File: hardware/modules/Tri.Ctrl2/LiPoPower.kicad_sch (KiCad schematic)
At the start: 26 parts, among them SW901 Power Switch, U901 INA226, U902 TPS63070RNMR, U903 INA226

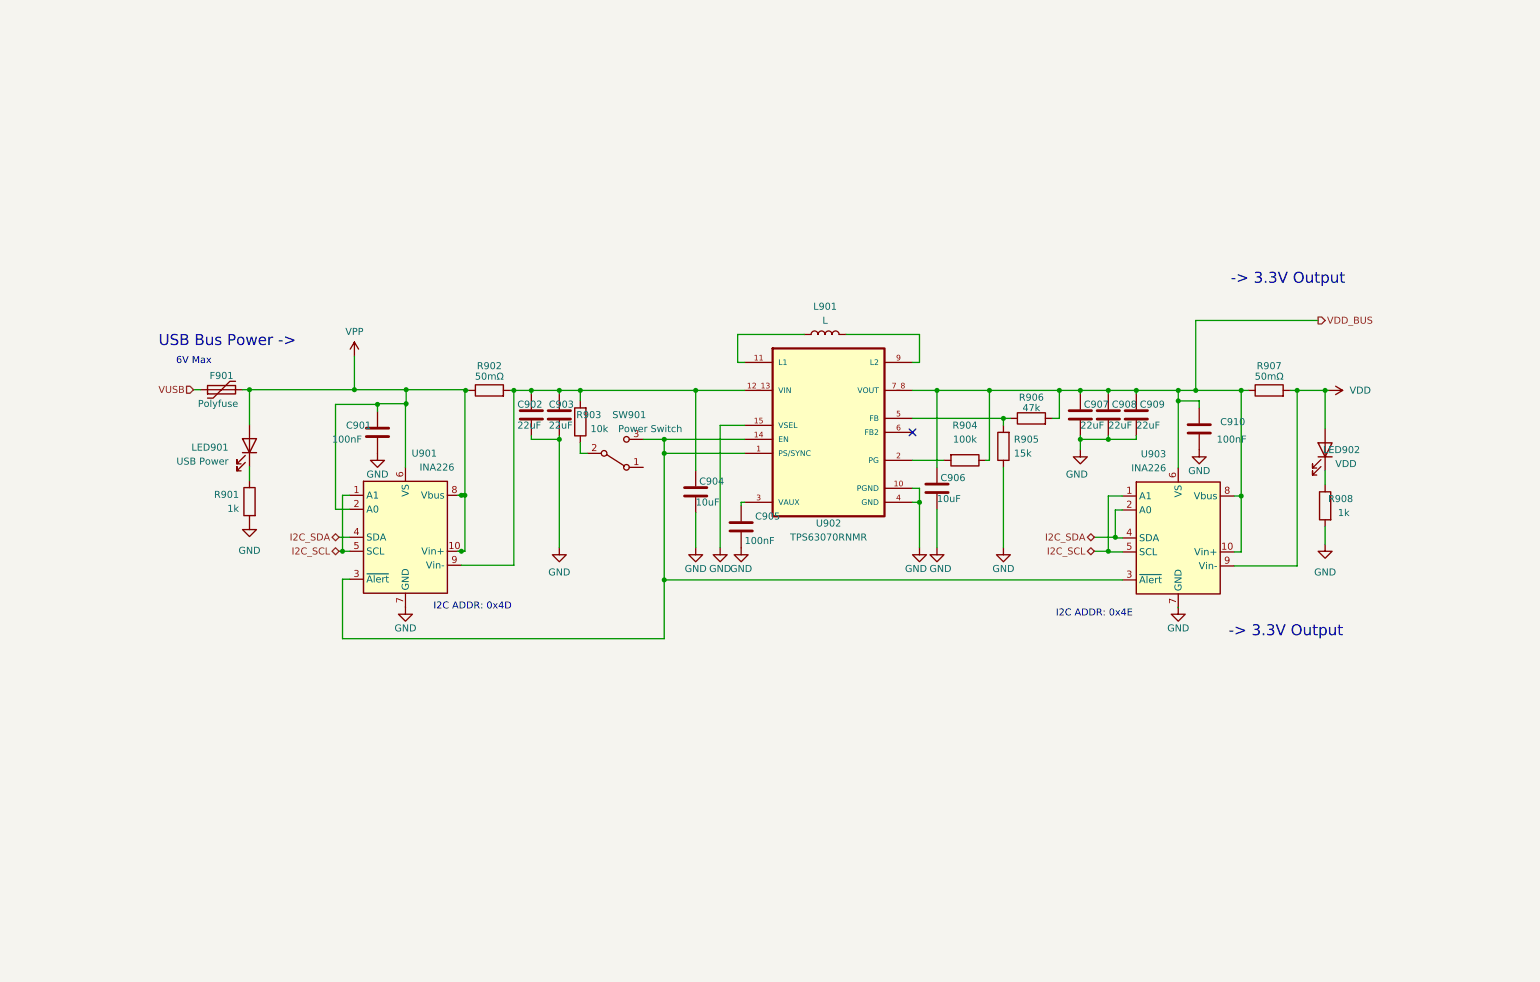
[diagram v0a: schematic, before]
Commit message: 回路図ひととおり完了
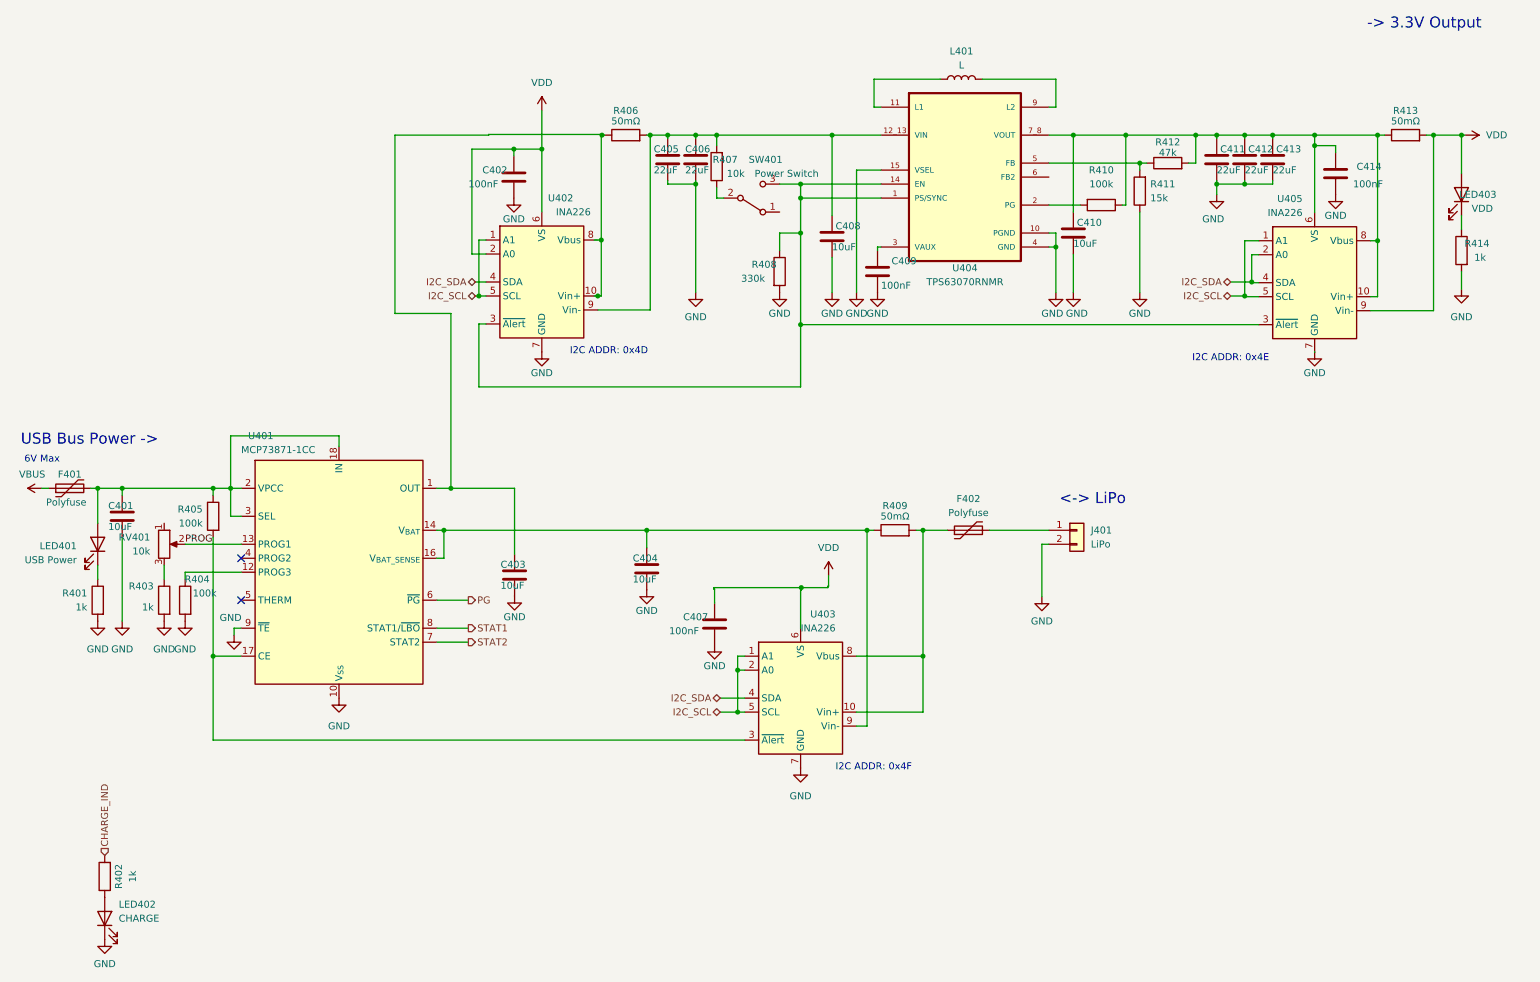
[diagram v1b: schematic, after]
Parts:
- removed C901, C905, C910: 100nF, Capacitor_SMD:C_0402_1005Metric, symbol Device:C
- removed C902, C903, C907, C908, C909: 22uF, Capacitor_SMD:C_0805_2012Metric, symbol Device:C
- removed C904, C906: 10uF, Capacitor_SMD:C_0603_1608Metric, symbol Device:C
- removed F901: Polyfuse, Fuse:Fuse_1206_3216Metric, symbol Device:Polyfuse
- removed L901: L, Inductor_SMD:L_Wuerth_WE-TPC-3816, symbol Device:L
- removed LED901: USB Power, LED_SMD:LED_0805_2012Metric, symbol Device:LED
- removed LED902: VDD, LED_SMD:LED_0805_2012Metric, symbol Device:LED
- removed R901, R908: 1k, Resistor_SMD:R_0402_1005Metric, symbol Device:R
- removed R902, R907: 50mΩ, Resistor_SMD:R_0805_2012Metric, symbol Device:R
- removed R903: 10k, Resistor_SMD:R_0402_1005Metric, symbol Device:R
- removed R904: 100k, Resistor_SMD:R_0402_1005Metric, symbol Device:R
- removed R905: 15k, Resistor_SMD:R_0402_1005Metric, symbol Device:R
- removed R906: 47k, Resistor_SMD:R_0402_1005Metric, symbol Device:R
- removed SW901: Power Switch, Button_Switch_THT:SW_Slide_SPDT_Angled_CK_OS102011MA1Q, symbol Switch:SW_SPDT
- removed U901, U903: INA226, Package_SO:VSSOP-10_3x3mm_P0.5mm, symbol Sensor_Energy:INA226
- removed U902: TPS63070RNMR, WOBCLibrary:VREG_TPS63070RNMR, symbol WOBCLibrary:TPS63070RNMR
- added C401, C403, C404, C408, C410: 10uF, Capacitor_SMD:C_0603_1608Metric, symbol Device:C
- added C402, C407, C409, C414: 100nF, Capacitor_SMD:C_0402_1005Metric, symbol Device:C
- added C405, C406, C411, C412, C413: 22uF, Capacitor_SMD:C_0805_2012Metric, symbol Device:C
- added F401, F402: Polyfuse, Fuse:Fuse_1206_3216Metric, symbol Device:Polyfuse
- added J401: LiPo, Connector_JST:JST_PH_S2B-PH-K_1x02_P2.00mm_Horizontal, symbol Connector_Generic:Conn_01x02
- added L401: L, Inductor_SMD:L_Wuerth_WE-TPC-3816, symbol Device:L
- added LED401: USB Power, LED_SMD:LED_0805_2012Metric, symbol Device:LED
- added LED402: CHARGE, LED_SMD:LED_0805_2012Metric, symbol Device:LED
- added LED403: VDD, LED_SMD:LED_0805_2012Metric, symbol Device:LED
- added R401, R402, R403, R414: 1k, Resistor_SMD:R_0402_1005Metric, symbol Device:R
- added R404, R405, R410: 100k, Resistor_SMD:R_0402_1005Metric, symbol Device:R
- added R406, R409, R413: 50mΩ, Resistor_SMD:R_0805_2012Metric, symbol Device:R
- added R407: 10k, Resistor_SMD:R_0402_1005Metric, symbol Device:R
- added R408: 330k, Resistor_SMD:R_0402_1005Metric, symbol Device:R
- added R411: 15k, Resistor_SMD:R_0402_1005Metric, symbol Device:R
- added R412: 47k, Resistor_SMD:R_0402_1005Metric, symbol Device:R
- added RV401: 10k, Potentiometer_SMD:Potentiometer_Bourns_TC33X_Vertical, symbol Device:R_Potentiometer
- added SW401: Power Switch, Button_Switch_THT:SW_CuK_OS102011MA1QN1_SPDT_Angled, symbol Switch:SW_SPDT
- added U401: MCP73871-1CC, Package_DFN_QFN:QFN-20-1EP_4x4mm_P0.5mm_EP2.5x2.5mm, symbol Battery_Management:MCP73871-1CC
- added U402, U403, U405: INA226, Package_SO:VSSOP-10_3x3mm_P0.5mm, symbol Sensor_Energy:INA226
- added U404: TPS63070RNMR, WOBCLibrary:VREG_TPS63070RNMR, symbol WOBCLibrary:TPS63070RNMR
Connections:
- net GND: now also C401.2, C402.2, C403.2, C404.2, C405.2, C406.2, C407.2, C408.2, C409.2, C410.2, C411.2, C412.2, C413.2, C414.2, J401.2 (Pin_2), LED402.1 (K), R401.2, R403.2, R404.2, R408.2, R411.1, R414.2, U401.10 (V_{SS}), U401.11 (V_{SS}), U401.21 (V_{SS}), U401.9 (~{TE}), U402.7 (GND), U403.7 (GND), U404.10 (PGND), U404.15 (VSEL), U404.4 (GND), U405.7 (GND)
- net I2C_SCL: now also U402.1 (A1), U402.5 (SCL), U403.1 (A1), U403.2 (A0), U403.5 (SCL), U405.1 (A1), U405.5 (SCL)
- net I2C_SDA: now also U402.4 (SDA), U403.4 (SDA), U405.2 (A0), U405.4 (SDA)
- net VDD: now also C402.1, C407.1, LED403.2 (A), R413.2, U402.2 (A0), U402.6 (VS), U403.6 (VS), U405.9 (Vin-)
- new net: C401.1, F401.2, LED401.2 (A), R405.1, U401.18 (IN), U401.19 (IN), U401.2 (VPCC), U401.3 (SEL)
- new net: C410.1, C411.1, C412.1, C413.1, C414.1, R410.1, R412.2, R413.1, U404.7_8 (VOUT), U405.10 (Vin+), U405.6 (VS), U405.8 (Vbus)
- new net: LED403.1 (K), R414.1
- new net: C405.1, C406.1, C408.1, R406.2, R407.2, U402.9 (Vin-), U404.12_13 (VIN)
- new net: C403.1, R406.1, U401.1 (OUT), U401.20 (OUT), U402.10 (Vin+)
- new net: R408.1, SW401.3 (C), U402.3 (~{Alert}), U404.1 (PS/SYNC), U404.14 (EN), U405.3 (~{Alert})
- new net: LED401.1 (K), R401.1
- new net: L401.1, U404.11 (L1)
- new net: L401.2, U404.9 (L2)
- new net: F402.2, J401.1 (Pin_1)
- new net: R411.2, R412.1, U404.5 (FB)
- new net: C409.1, U404.3 (VAUX)
- new net: C404.1, R409.1, U401.14 (V_{BAT}), U401.15 (V_{BAT}), U401.16 (V_{BAT_SENSE}), U403.9 (Vin-)
- new net: F402.1, R409.2, U403.10 (Vin+), U403.8 (Vbus)
- new net: R403.1, RV401.3
- new net: LED402.2 (A), R402.1
- new net: R410.2, U404.2 (PG)
- new net: R407.1, SW401.2 (B)
- new net: R405.2, U401.17 (CE), U403.3 (~{Alert})
- new net: R404.1, U401.12 (PROG3)
- new net CHARGE_IND: R402.2
- new net PG: U401.6 (~{PG})
- new net PROG: RV401.2, U401.13 (PROG1)
- new net STAT1: U401.8 (STAT1/~{LBO})
- new net STAT2: U401.7 (STAT2)
- new net VBUS: F401.1
- no-connect marks 1 -> 2
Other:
- note added: "<-> LiPo"
- note added: "I2C ADDR: 0x4F"

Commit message: ひととおり配置
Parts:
- J401: footprint Connector_JST:JST_PH_S2B-PH-K_1x02_P2.00mm_Horizontal -> Connector_JST:JST_XA_S02B-XASK-1N-BN_1x02_P2.50mm_Horizontal
- SW401: footprint Button_Switch_THT:SW_CuK_OS102011MA1QN1_SPDT_Angled -> Button_Switch_THT:SW_Slide_SPDT_Straight_CK_OS102011MS2Q
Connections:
- net VDD: now also C414.1, U405.6 (VS)
- net at C410.1, C411.1, C412.1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: no longer C414.1, U405.6 (VS)
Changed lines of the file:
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@@
 	)
 	(junction
-		(at 248.92 37.465)
-		(diameter 0)
-		(color 0 0 0 0)
-	)
-	(junction
 		(at 231.14 46.355)
 		(diameter 0)
@@
 	)
 	(junction
+		(at 248.92 39.37)
+		(diameter 0)
+		(color 0 0 0 0)
+	)
+	(junction
 		(at 32.385 101.6)
 		(diameter 0)
@@
 	)
 	(junction
-		(at 248.92 39.37)
-		(diameter 0)
-		(color 0 0 0 0)
-	)
-	(junction
 		(at 177.8 109.22)
 		(diameter 0)
@@
 	(wire
 		(pts
+			(xy 248.92 34.29) (xy 248.92 39.37)
+		)
+		(stroke
+			(width 0)
+			(type default)
+		)
+	)
+	(wire
+		(pts
 			(xy 98.425 71.755) (xy 97.155 71.755)
 		)
@@
 	(wire
 		(pts
-			(xy 248.92 37.465) (xy 260.35 37.465)
-		)
-		(stroke
-			(width 0)
-			(type default)
-		)
-	)
-	(wire
-		(pts
 			(xy 260.35 37.465) (xy 261.62 37.465)
 		)
@@
 	(wire
 		(pts
-			(xy 248.92 37.465) (xy 248.92 39.37)
-		)
-		(stroke
-			(width 0)
-			(type default)
-		)
-	)
-	(wire
-		(pts
 			(xy 168.91 27.305) (xy 168.91 32.385)
 		)
@@
 	(wire
 		(pts
-			(xy 241.3 37.465) (xy 248.92 37.465)
+			(xy 241.3 37.465) (xy 260.35 37.465)
 		)
 		(stroke
@@
 			)
 		)
-		(property "Footprint" "Connector_JST:JST_PH_S2B-PH-K_1x02_P2.00mm_Horizontal"
+		(property "Footprint" "Connector_JST:JST_XA_S02B-XASK-1N-BN_1x02_P2.50mm_Horizontal"
 			(at 205.74 109.22 0)
 			(effects
@@
 	)
 	(symbol
+		(lib_name "VDD_3")
+		(lib_id "power:VDD")
+		(at 248.92 34.29 0)
+		(unit 1)
+		(exclude_from_sim no)
+		(in_bom yes)
+		(on_board yes)
+		(dnp no)
+		(fields_autoplaced yes)
+		(property "Reference" "#PWR0431"
+			(at 248.92 38.1 0)
+			(effects
+				(font
+					(size 1.27 1.27)
+				)
+				(hide yes)
+			)
+		)
+		(property "Value" "VDD"
+			(at 248.92 29.21 0)
+			(effects
+				(font
+					(size 1.27 1.27)
+				)
+			)
+		)
+		(property "Footprint" ""
+			(at 248.92 34.29 0)
+			(effects
+				(font
+					(size 1.27 1.27)
+				)
+				(hide yes)
+			)
+		)
+		(property "Datasheet" ""
+			(at 248.92 34.29 0)
+			(effects
+				(font
+					(size 1.27 1.27)
+				)
+				(hide yes)
+			)
+		)
+		(property "Description" "Power symbol creates a global label with name \"VDD\""
+			(at 248.92 34.29 0)
+			(effects
+				(font
+					(size 1.27 1.27)
+				)
+				(hide yes)
+			)
+		)
+		(pin "1"
+		)
+		(instances
+			(project ""
+				(path "/80fbddc6-aa50-4ba3-b7b9-21fad44f05f1/aff5d149-7d1f-44c5-87f1-7b19a74f6f79"
+					(reference "#PWR0431")
+					(unit 1)
+				)
+			)
+		)
+	)
+	(symbol
 		(lib_id "power:VDD")
 		(at 276.225 37.465 270)
@@
 			)
 		)
-		(property "Description" "\nWide input voltage (2V-16V) buck-boost converter\n"
+		(property "Description" "Wide input voltage (2V-16V) buck-boost converter"
 			(at 184.15 -2.175 0)
 			(effects
@@
 			)
 		)
-		(property "Footprint" "Button_Switch_THT:SW_CuK_OS102011MA1QN1_SPDT_Angled"
+		(property "Footprint" "Button_Switch_THT:SW_Slide_SPDT_Straight_CK_OS102011MS2Q"
 			(at 146.685 48.895 0)
 			(effects

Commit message: ひととおり配線
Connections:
- net at C403.1, R406.1, U401.1 (OUT)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: now also U402.8 (Vbus)
- no-connect marks 2 -> 4
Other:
- moved on the sheet: U402
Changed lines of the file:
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@@
-	)
-	(junction
-		(at 108.585 40.005)
-		(diameter 0)
-		(color 0 0 0 0)
 	)
 	(junction
@@
 	)
 	(junction
+		(at 107.95 40.005)
+		(diameter 0)
+		(color 0 0 0 0)
+	)
+	(junction
 		(at 155.702 119.634)
 		(diameter 0)
@@
 	)
 	(junction
-		(at 118.745 66.675)
-		(diameter 0)
-		(color 0 0 0 0)
-	)
-	(junction
 		(at 48.895 132.08)
 		(diameter 0)
@@
 		(diameter 0)
 		(color 0 0 0 0)
+	)
+	(no_connect
+		(at 40.005 107.95)
 	)
 	(no_connect
@@
 	)
 	(no_connect
+		(at 200.66 45.085)
+	)
+	(no_connect
 		(at 53.975 121.92)
 	)
 	(wire
 		(pts
+			(xy 107.95 76.835) (xy 108.585 76.835)
+		)
+		(stroke
+			(width 0)
+			(type default)
+		)
+	)
+	(wire
+		(pts
 			(xy 199.39 111.76) (xy 200.66 111.76)
 		)
@@
 	(wire
 		(pts
-			(xy 98.425 71.755) (xy 97.155 71.755)
+			(xy 97.79 71.755) (xy 97.155 71.755)
 		)
 		(stroke
@@
 	(wire
 		(pts
-			(xy 98.425 56.515) (xy 97.155 56.515)
+			(xy 97.79 56.515) (xy 97.155 56.515)
 		)
 		(stroke
@@
 	(wire
 		(pts
-			(xy 98.425 59.055) (xy 95.885 59.055)
+			(xy 97.79 59.055) (xy 95.885 59.055)
+		)
+		(stroke
+			(width 0)
+			(type default)
+		)
+	)
+	(wire
+		(pts
+			(xy 107.95 40.005) (xy 108.585 40.005)
 		)
 		(stroke
@@
 	(wire
 		(pts
-			(xy 108.585 40.005) (xy 108.585 51.435)
+			(xy 107.95 40.005) (xy 107.95 51.435)
 		)
 		(stroke
@@
 	(wire
 		(pts
-			(xy 118.11 66.675) (xy 118.745 66.675)
+			(xy 118.11 66.675) (xy 119.38 66.675)
 		)
 		(stroke
@@
 	(wire
 		(pts
-			(xy 96.52 64.135) (xy 98.425 64.135)
+			(xy 96.52 64.135) (xy 97.79 64.135)
 		)
 		(stroke
@@
 	(wire
 		(pts
-			(xy 118.745 66.675) (xy 119.38 66.675)
-		)
-		(stroke
-			(width 0)
-			(type default)
-		)
-	)
-	(wire
-		(pts
 			(xy 200.66 42.545) (xy 217.17 42.545)
 		)
@@
 	(wire
 		(pts
-			(xy 118.745 69.215) (xy 128.27 69.215)
+			(xy 118.11 69.215) (xy 128.27 69.215)
 		)
 		(stroke
@@
 	(wire
 		(pts
-			(xy 103.505 40.005) (xy 108.585 40.005)
+			(xy 103.505 40.005) (xy 107.95 40.005)
 		)
 		(stroke
@@
 	(wire
 		(pts
-			(xy 97.155 66.675) (xy 98.425 66.675)
+			(xy 97.155 66.675) (xy 97.79 66.675)
 		)
 		(stroke
@@
 	(symbol
 		(lib_id "Sensor_Energy:INA226")
-		(at 108.585 64.135 0)
+		(at 107.95 64.135 0)
 		(mirror y)
 		(unit 1)
@@
 		(dnp no)
 		(property "Reference" "U402"
-			(at 114.3 48.895 0)
+			(at 113.665 48.895 0)
 			(effects
 				(font
@@
 		)
 		(property "Value" "INA226"
-			(at 117.475 51.435 0)
+			(at 116.84 51.435 0)
 			(effects
 				(font
@@
 		)
 		(property "Footprint" "Package_SO:VSSOP-10_3x3mm_P0.5mm"
-			(at 88.265 75.565 0)
+			(at 87.63 75.565 0)
 			(effects
 				(font
@@
 		)
 		(property "Datasheet" "http://www.ti.com/lit/ds/symlink/ina226.pdf"
-			(at 99.695 66.675 0)
+			(at 99.06 66.675 0)
 			(effects
 				(font
@@
 		)
 		(property "Description" ""
-			(at 108.585 64.135 0)
+			(at 107.95 64.135 0)
 			(effects
 				(font
@@
 		)
 		(property "LCSC" "C49851"
-			(at 108.585 64.135 0)
-			(effects
-				(font
+			(at 107.95 64.135 0)
+			(effects
+				(font

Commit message: THERMに10kの抵抗
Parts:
- added R405: 10k, Resistor_SMD:R_0402_1005Metric, symbol Device:R
- renumbered R405 to R406, R406 to R407, R407 to R408, R408 to R409, R409 to R410, R410 to R411, R411 to R412, R412 to R413, R413 to R414, R414 to R415
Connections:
- net GND: now also R405.2
- net at U401.5 (THERM): now also R405.1
- no-connect marks 4 -> 3

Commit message: LCSC最終確認
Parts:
- F401, F402: LCSC C883133 -> C883133
- R409: LCSC C23137 -> C25778
- U401: LCSC C511310 -> C511310
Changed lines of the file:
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@@
 			)
 		)
-		(property "LCSC" "C23137"
+		(property "LCSC" "C25778"
 			(at 151.765 62.23 0)
 			(effects
@@
 			)
 		)
-		(property "LCSC" " C883133"
+		(property "LCSC" "C883133"
 			(at 22.86 101.6 0)
 			(effects
@@
 			)
 		)
-		(property "LCSC" " C883133"
+		(property "LCSC" "C883133"
 			(at 186.055 109.22 0)
 			(effects
@@
 			)
 		)
-		(property "LCSC" " C511310"
+		(property "LCSC" "C511310"
 			(at 71.755 116.84 0)
 			(effects
